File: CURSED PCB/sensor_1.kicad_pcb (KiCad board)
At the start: 4 copper layers, 42 x 40 mm, 83 parts, among them J1 Debugging Connector, J2 Micro_SD_Card, J3 Gecko Connector, J5 G125-MH104M4-04AD000P, U1 STM32G431KBT6, U10 MCP2562, U11 TPS61046YFFR, U12 AD5761BRUZ, U2 INA180-A3, U3 MIC94090YC6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

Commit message: footprint folde rupdate
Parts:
- C19: footprint Capacitor_SMD:C_0805_2012Metric_Pad1.18x1.45mm_HandSolder -> EMK107B7105KA-T:CAPC1608X90N
- C20: footprint Capacitor_SMD:C_0805_2012Metric_Pad1.18x1.45mm_HandSolder -> MCASU31LSB5105KTNA01:CAPC3216X180N
- F1: footprint Fuse:Fuse_Bourns_MF-RG300 -> Fuse:Fuse_1206_3216Metric_Pad1.42x1.75mm_HandSolder
- moved F1 2.70 mm to (49.4, 40.0)
- moved 5VTP1 0.63 mm to (60.5, 39.7)
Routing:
- net +3.3VD: track 116.2 -> 128.8 mm, vias 14 -> 15
- net Net-(J5-+5V): track 10.2 -> 7.90 mm
- net Net-(U2-+): track 8.65 -> 10.2 mm
- net GND: vias 54 -> 55

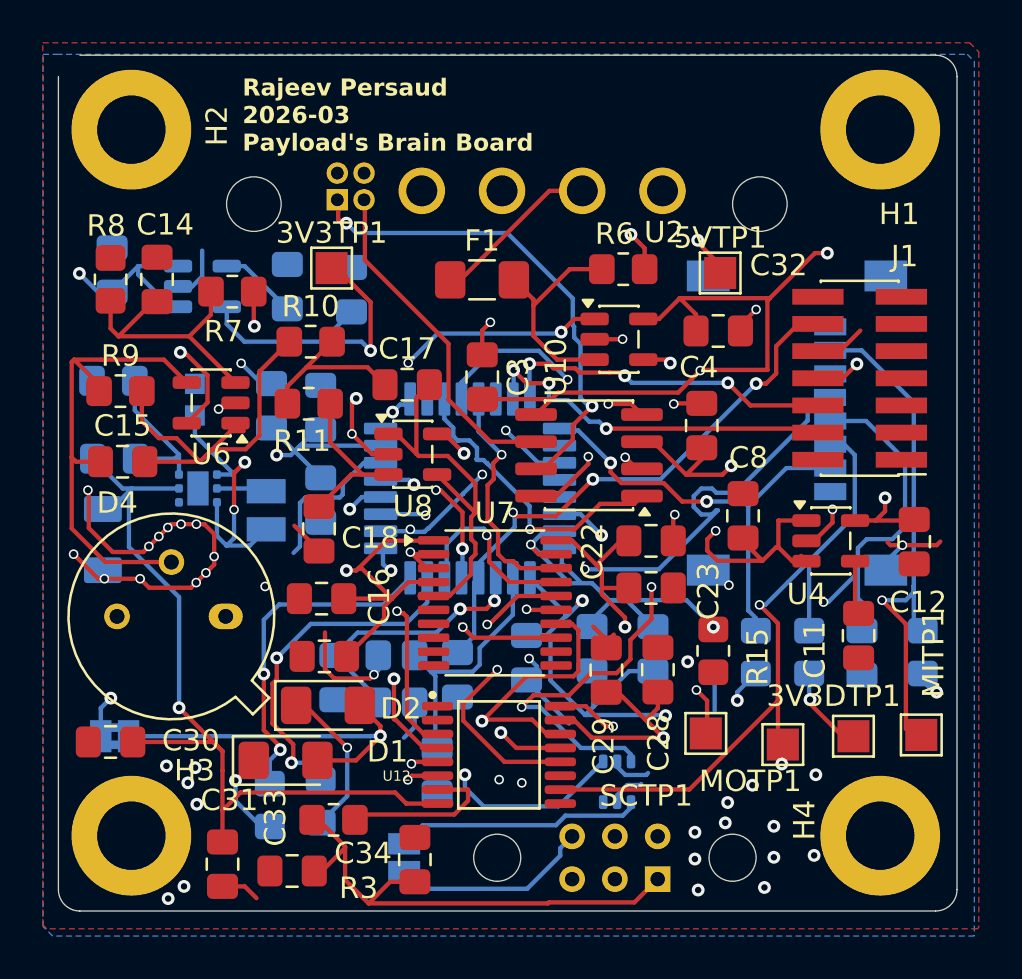
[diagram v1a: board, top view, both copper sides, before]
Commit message: updates traces and footprints
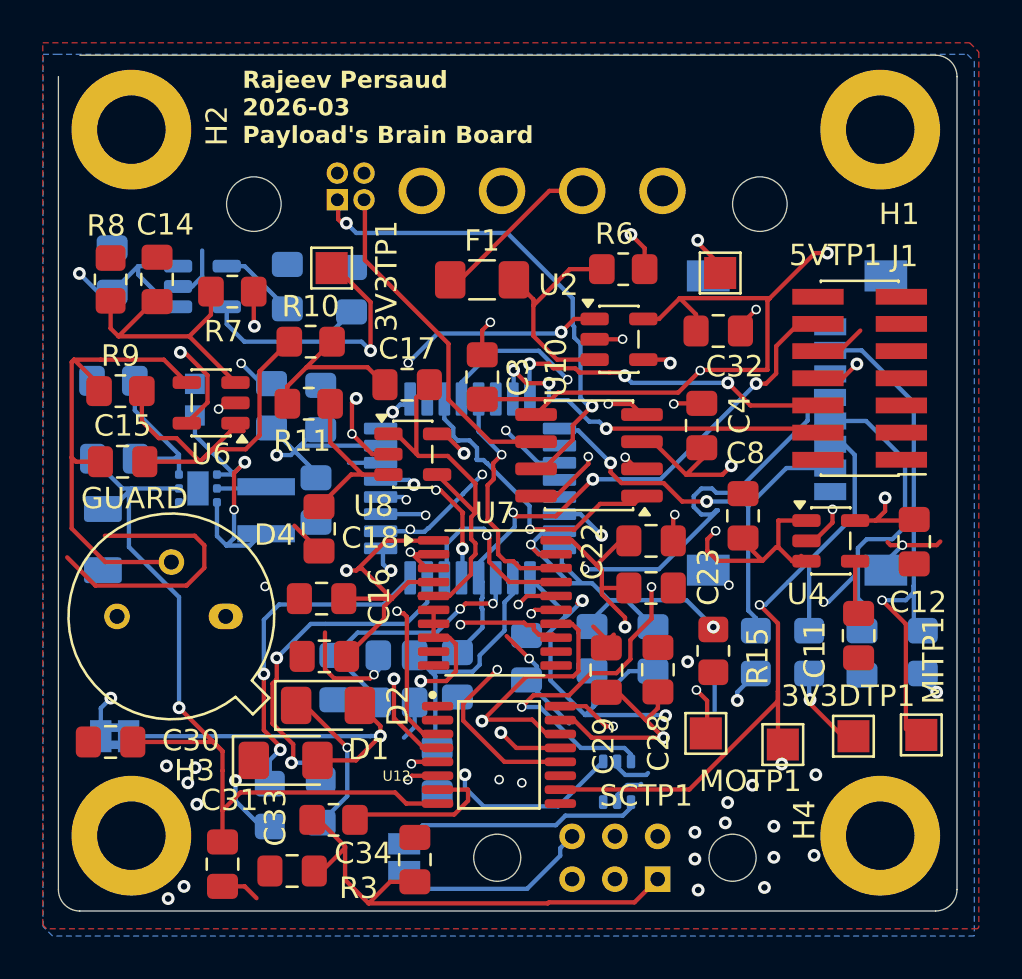
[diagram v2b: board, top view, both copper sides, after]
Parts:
- C15: value 3200nF -> 6500nF
- C17: value 47nF -> 100nF
- C18: value 20nF -> 43nF
- L1: footprint LBM2016T120J:INDC2016X180N -> ul_NRH3010T100MN:IND_TAIYO_NRH3010_TAY
- R10: value 986 -> 2.9k
- R11: value 2.23k -> 6.3k
- moved C24 0.22 mm to (41.6, 50.3)
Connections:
- U7 pad 6: unconnected-(U7-CH1-Pad6) -> GND
- U7 pad 7: unconnected-(U7-CH2-Pad7) -> GND
- U7 pad 8: unconnected-(U7-CH3-Pad8) -> GND
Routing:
- net GND: track 116.2 -> 99.6 mm, vias 55 -> 44
- net (no net): track 0.00 -> 13.2 mm
- net /MOSI: track 57.4 -> 54.4 mm
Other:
- board text added: "GUARD"

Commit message: drc errors
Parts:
- R15: moved to B.Cu
- moved R15 5.48 mm to (54.7, 57.2)
- moved C25 3.20 mm to (57.7, 57.3)
- moved C26 2.60 mm to (60.0, 57.3)
- moved 5VTP1 1.00 mm to (59.5, 39.4)
- moved C24 0.57 mm to (42.2, 50.3)
- moved C17 0.34 mm to (45.9, 44.6)
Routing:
- net (no net): track 13.2 -> 0.00 mm
- net GND: track 99.6 -> 94.3 mm, vias 44 -> 46
- net +5V: track 76.6 -> 81.7 mm
- net +3.3VD: track 128.8 -> 131.5 mm
- net /MOSI: track 54.4 -> 55.5 mm
- net /CUR_SEN: track 22.0 -> 22.7 mm
- net +3.3VA: track 65.1 -> 65.6 mm

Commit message: updated booster
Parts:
- removed U11: TPS61046YFFR, Package_SON:WSON-6-1EP_2x2mm_P0.65mm_EP1x1.6mm
- added U9: TLV61046ADBVR, TLV61046A:SOT95P280X145-6N, B.Cu at (35.0, 45.8)
- moved C19 2.29 mm to (38.3, 45.8)
- moved R12 1.64 mm to (32.1, 43.1)
- moved C6 0.61 mm to (40.2, 45.9)
- moved C7 0.35 mm to (42.2, 46.0)
- moved R13 0.32 mm to (32.5, 48.6), turned to 0 degrees
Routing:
- net +24V: track 39.7 -> 48.8 mm, vias 1 -> 3
- net GND: track 94.3 -> 99.0 mm, vias 46 -> 65
- net Net-(U9-SW): track 2.63 -> 7.14 mm
- net +5V: track 81.7 -> 83.6 mm, vias 12 -> 14
- net Net-(U9-FB): track 7.34 -> 8.69 mm

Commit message: small changes
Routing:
- net +24V: track 48.8 -> 44.1 mm
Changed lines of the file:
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@@
 	)
 	(gr_line
+		(start 31.5525 48.52)
+		(end 30.41 48.52)
+		(stroke
+			(width 1.0032)
+			(type default)
+		)
+		(layer "F.Mask")
+	)
+	(gr_line
 		(start 31.49 44.92)
 		(end 30.32 43.75)
@@
 	)
 	(segment
-		(start 34.077146 44.2142)
-		(end 32.902854 44.2142)
-		(width 0.2032)
-		(layer "F.Cu")
-		(net 22)
-	)
-	(segment
-		(start 32.902854 44.2142)
-		(end 32.51 44.607054)
-		(width 0.2032)
-		(layer "F.Cu")
-		(net 22)
-	)
-	(segment
-		(start 34.3958 44.532854)
-		(end 34.077146 44.2142)
-		(width 0.2032)
-		(layer "F.Cu")
-		(net 22)
-	)
-	(segment
-		(start 34.3958 45.725012)
-		(end 34.3958 44.532854)
-		(width 0.2032)
-		(layer "F.Cu")
-		(net 22)
-	)
-	(segment
-		(start 34.758525 46.087737)
-		(end 34.3958 45.725012)
-		(width 0.2032)
-		(layer "F.Cu")
-		(net 22)
-	)
-	(segment
 		(start 37.26 62.96)
 		(end 37.26 62.05)
@@
 		(net 22)
 	)
-	(segment
-		(start 32.51 44.607054)
-		(end 32.51 46.95)
-		(width 0.2032)
-		(layer "F.Cu")
-		(net 22)
-	)
 	(via
 		(at 34.758525 46.087737)
@@
 	)
 	(via
-		(at 35.23 60.02)
+		(at 34.758525 49.90625)
 		(size 0.6)
 		(drill 0.3)
@@
 	)
 	(via
-		(at 32.51 46.95)
-		(size 0.45)
+		(at 35.23 60.02)
+		(size 0.6)
 		(drill 0.3)
 		(layers "F.Cu" "B.Cu")
@@
 	)
 	(segment
-		(start 32.51 46.95)
-		(end 32.51 48.58)
-		(width 0.2032)
-		(layer "B.Cu")
-		(net 22)
-	)
-	(segment
 		(start 36.2375 45.82)
 		(end 35.026262 45.82)
@@
 	)
 	(segment
-		(start 32.51 48.58)
-		(end 32.51 49.32)
+		(start 32.88625 49.90625)
+		(end 34.70625 49.90625)
 		(width 0.2032)
 		(layer "B.Cu")
@@
 	)
 	(segment
-		(start 32.88625 49.90625)
-		(end 34.70625 49.90625)
+		(start 34.82 46.149212)
+		(end 34.758525 46.087737)
 		(width 0.2032)
-		(layer "B.Cu")
+		(layer "In1.Cu")
+		(net 22)
+	)
+	(segment
+		(start 34.758525 49.90625)
+		(end 34.82 49.844775)
+		(width 0.2032)
+		(layer "In1.Cu")
+		(net 22)
+	)
+	(segment
+		(start 34.82 49.844775)
+		(end 34.82 46.149212)
+		(width 0.2032)
+		(layer "In1.Cu")
 		(net 22)
 	)

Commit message: cleaned upa  trace
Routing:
- net GND: track 99.0 -> 107.1 mm, vias 65 -> 77
- net +5V: track 83.6 -> 77.7 mm, vias 14 -> 13
- net /MCU/CS_DAC: track 18.5 -> 20.2 mm
- net /MKLKIN: track 11.2 -> 10.5 mm
- net /TXD: track 14.4 -> 13.8 mm
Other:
- outline, holes or cut-outs redrawn

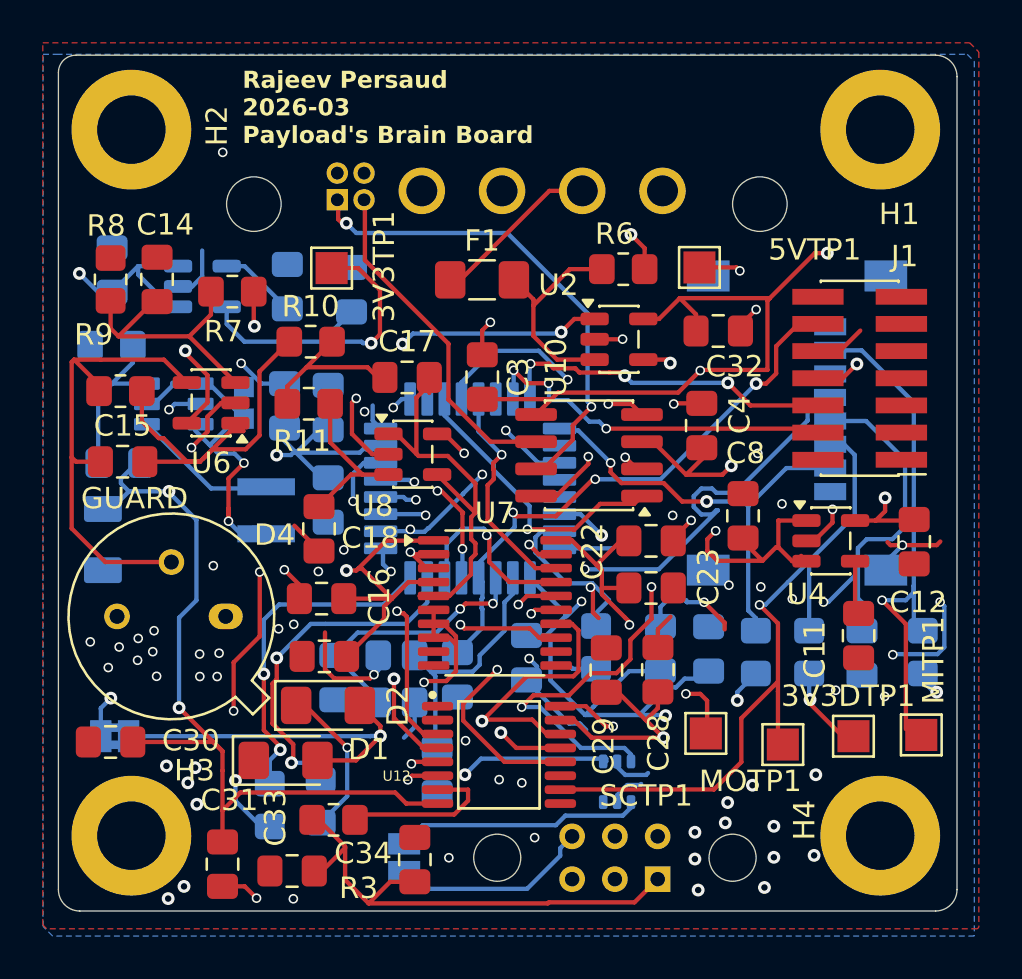
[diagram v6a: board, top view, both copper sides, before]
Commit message: updated misiing datasheet rdy for review
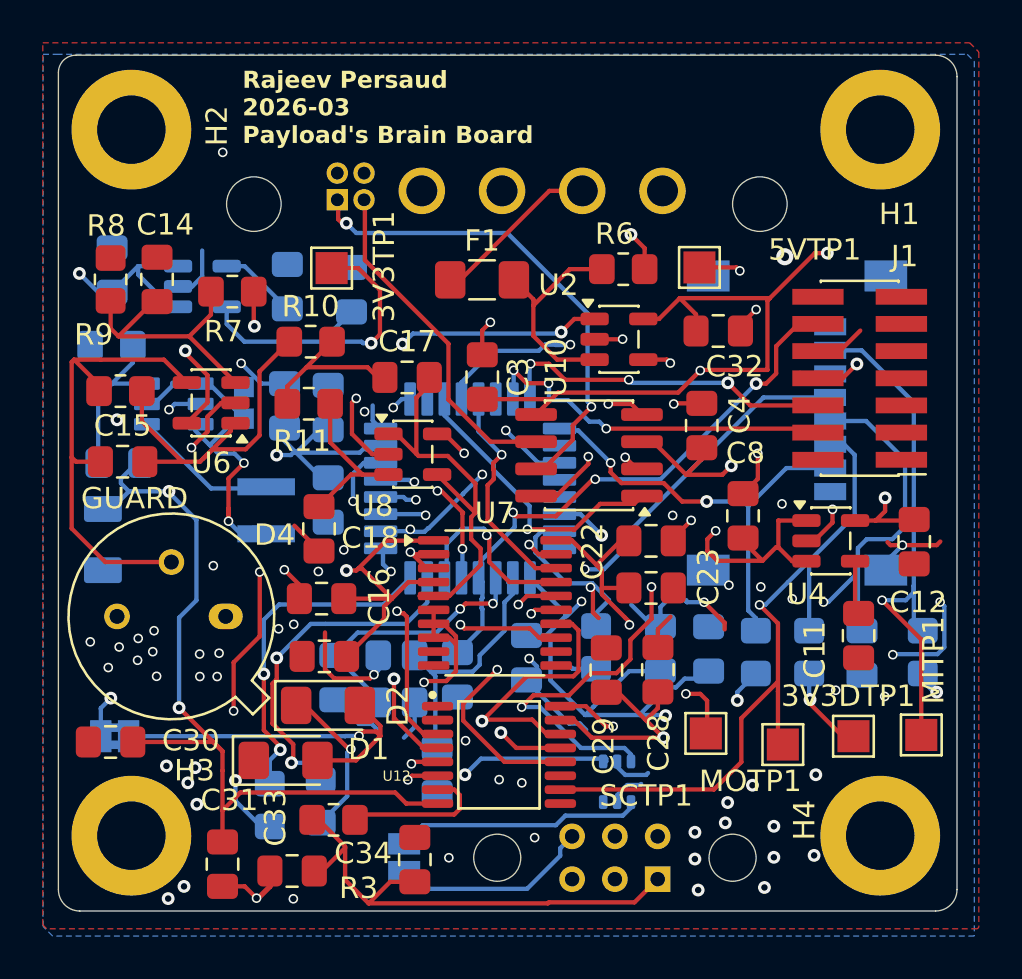
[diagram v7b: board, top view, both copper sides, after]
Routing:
- net GND: track 107.1 -> 112.8 mm, vias 77 -> 79
- net /SCLK: track 67.7 -> 64.7 mm
- net /Amplifer/anti-aliasing filter/VIN: track 18.7 -> 17.2 mm
- net /RXD: track 11.1 -> 11.9 mm
- net Net-(U12-VOUT): track 7.60 -> 6.90 mm
- net /MISO: track 64.7 -> 65.3 mm

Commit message: extra cleanup while waiting for review
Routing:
- net /Power/CANH: track 23.0 -> 39.3 mm
- net GND: track 112.8 -> 120.0 mm
- net /MKLKIN: track 10.5 -> 12.0 mm, vias 1 -> 2
